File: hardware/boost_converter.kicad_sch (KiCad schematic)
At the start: 12 parts, among them U4 SparkFun_LiPower, U5 TPS61200DRC

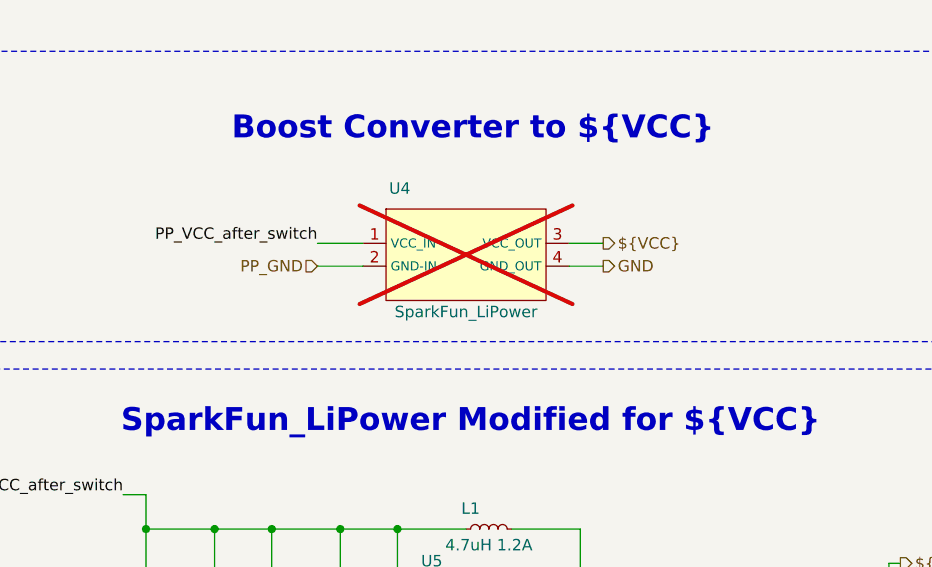
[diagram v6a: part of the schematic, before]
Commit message: Completed the property teble except for the cyristal oscilator
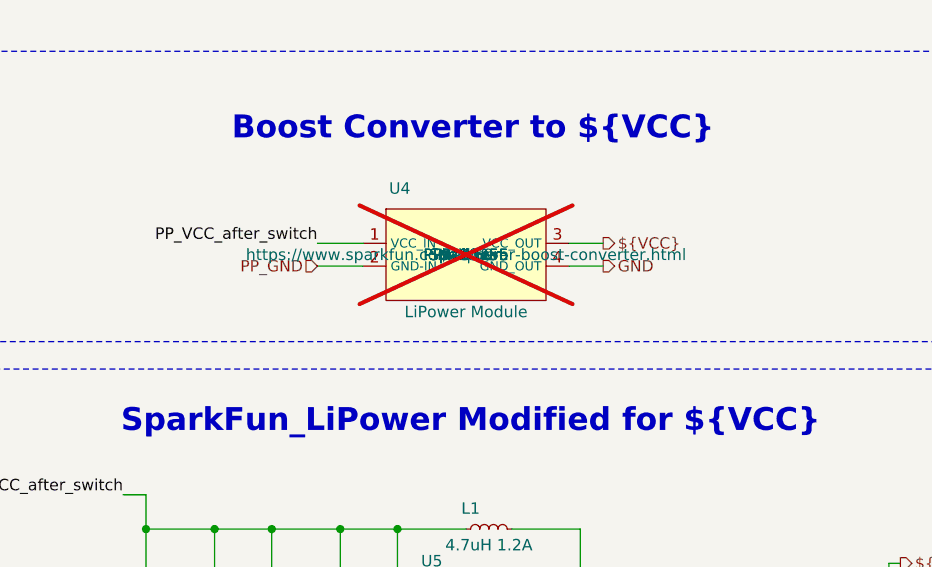
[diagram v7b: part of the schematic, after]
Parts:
- R5, R6, R7, R8: footprint (none) -> ~
- S1: Package (none) -> SMD
- U4: value SparkFun_LiPower -> LiPower Module; Manuf. Name (none) -> SparkFun; Manuf. Part # (none) -> PRT-10255; Package (none) -> Module; Supplier Link (none) -> https://www.sparkfun.com/lipower-boost-converter.html; Supplier Name (none) -> SparkFun; Supplier Part # (none) -> PRT-10255; Supplier Unit Price (none) -> $20.59
- U5: Supplier Name JLCPCB -> (none); Supplier Unit Price $1.4430 -> (none)

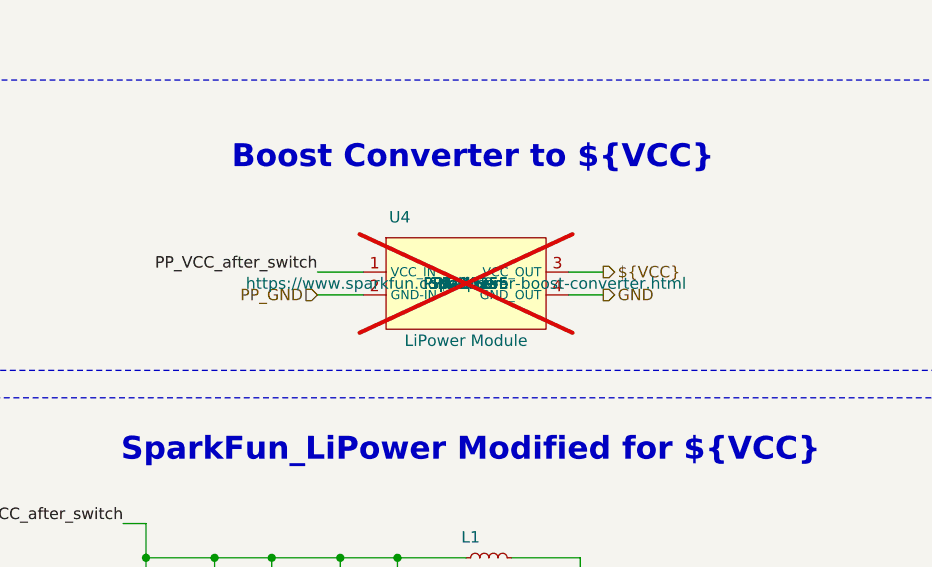
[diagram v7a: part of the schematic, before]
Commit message: Made some small changes on the properties of some components while having last weeks meeting and added the fp-info-cache to the gitignore file
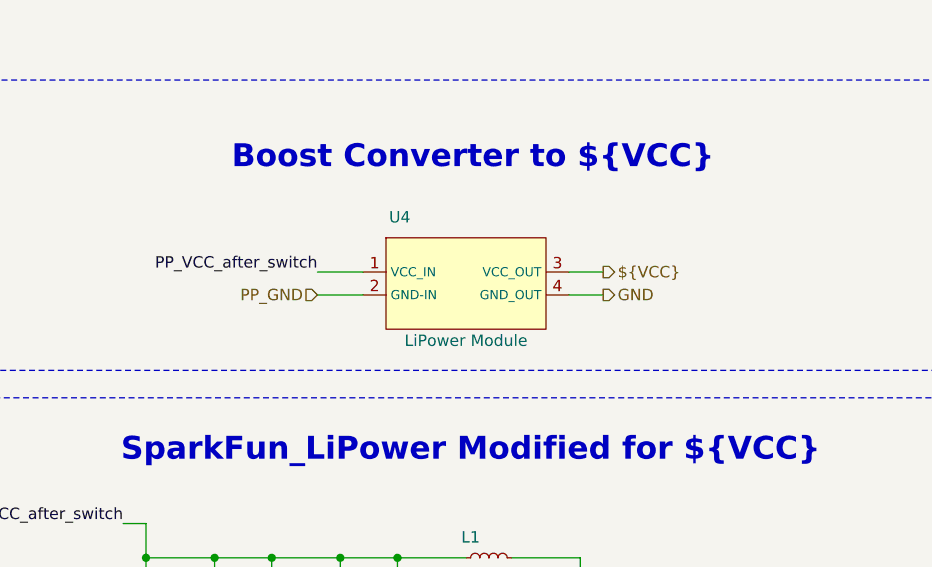
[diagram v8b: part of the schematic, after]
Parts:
- L1: footprint (none) -> ~
- U4: now fitted
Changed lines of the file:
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@@
 					(size 1.27 1.27)
 				)
+				(hide yes)
 			)
 		)
@@
 					(size 1.27 1.27)
 				)
+				(hide yes)
 			)
 		)
@@
 					(size 1.27 1.27)
 				)
+				(hide yes)
 			)
 		)
@@
 					(size 1.27 1.27)
 				)
+				(hide yes)
 			)
 		)
@@
 					(size 1.27 1.27)
 				)
+				(hide yes)
 			)
 		)
@@
 					(size 1.27 1.27)
 				)
+				(hide yes)
 			)
 		)
@@
 			)
 		)
-		(property "Footprint" ""
+		(property "Footprint" "~"
 			(at 149.86 114.3 0)
 			(effects
@@
 					(size 1.27 1.27)
 				)
+				(hide yes)
 			)
 		)
@@
 					(size 1.27 1.27)
 				)
+				(hide yes)
 			)
 		)
@@
 					(size 1.27 1.27)
 				)
+				(hide yes)
 			)
 		)
@@
 					(size 1.27 1.27)
 				)
+				(hide yes)
 			)
 		)
@@
 					(size 1.27 1.27)
 				)
+				(hide yes)
 			)
 		)
@@
 					(size 1.27 1.27)
 				)
+				(hide yes)
 			)
 		)
@@
 					(size 1.27 1.27)
 				)
+				(hide yes)
 			)
 		)
@@
 					(size 1.27 1.27)
 				)
+				(hide yes)
 			)
 		)
@@
 					(size 1.27 1.27)
 				)
+				(hide yes)
 			)
 		)
@@
 					(size 1.27 1.27)
 				)
+				(hide yes)
 			)
 		)
@@
 					(size 1.27 1.27)
 				)
+				(hide yes)
 			)
 		)
@@
 					(size 1.27 1.27)
 				)
+				(hide yes)
 			)
 		)
@@
 					(size 1.27 1.27)
 				)
+				(hide yes)
 			)
 		)
@@
 					(size 1.27 1.27)
 				)
+				(hide yes)
 			)
 		)
@@
 					(size 1.27 1.27)
 				)
+				(hide yes)
 			)
 		)
@@
 					(size 1.27 1.27)
 				)
+				(hide yes)
 			)
 		)
@@
 					(size 1.27 1.27)
 				)
+				(hide yes)
 			)
 		)
@@
 					(size 1.27 1.27)
 				)
+				(hide yes)
 			)
 		)
@@
 		(in_bom no)
 		(on_board yes)
-		(dnp yes)
+		(dnp no)
 		(property "Reference" "U4"
 			(at 139.954 76.454 0)
@@
 					(size 1.27 1.27)
 				)
+				(hide yes)
 			)
 		)
@@
 					(size 1.27 1.27)
 				)
+				(hide yes)
 			)
 		)
@@
 					(size 1.27 1.27)
 				)
+				(hide yes)
 			)
 		)
@@
 					(size 1.27 1.27)
 				)
+				(hide yes)
 			)
 		)
@@
 					(size 1.27 1.27)
 				)
+				(hide yes)
 			)
 		)
@@
 					(size 1.27 1.27)
 				)
+				(hide yes)
 			)
 		)
@@
 					(size 1.27 1.27)
 				)
+				(hide yes)
 			)
 		)
@@
 					(size 1.27 1.27)
 				)
+				(hide yes)
 			)
 		)
@@
 					(size 1.27 1.27)
 				)
+				(hide yes)
 			)
 		)
@@
 					(size 1.27 1.27)
 				)
+				(hide yes)
 			)
 		)
@@
 					(size 1.27 1.27)
 				)
+				(hide yes)
 			)
 		)
@@
 					(size 1.27 1.27)
 				)
+				(hide yes)
 			)
 		)
@@
 					(size 1.27 1.27)
 				)
+				(hide yes)
 			)
 		)
@@
 					(size 1.27 1.27)
 				)
+				(hide yes)
 			)
 		)
@@
 					(size 1.27 1.27)
 				)
-			)
-		)
+				(hide yes)
+			)
+		)
